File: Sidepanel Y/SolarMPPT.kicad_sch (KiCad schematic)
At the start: 38 parts, among them U11 INA180A4, U12 INA180A4

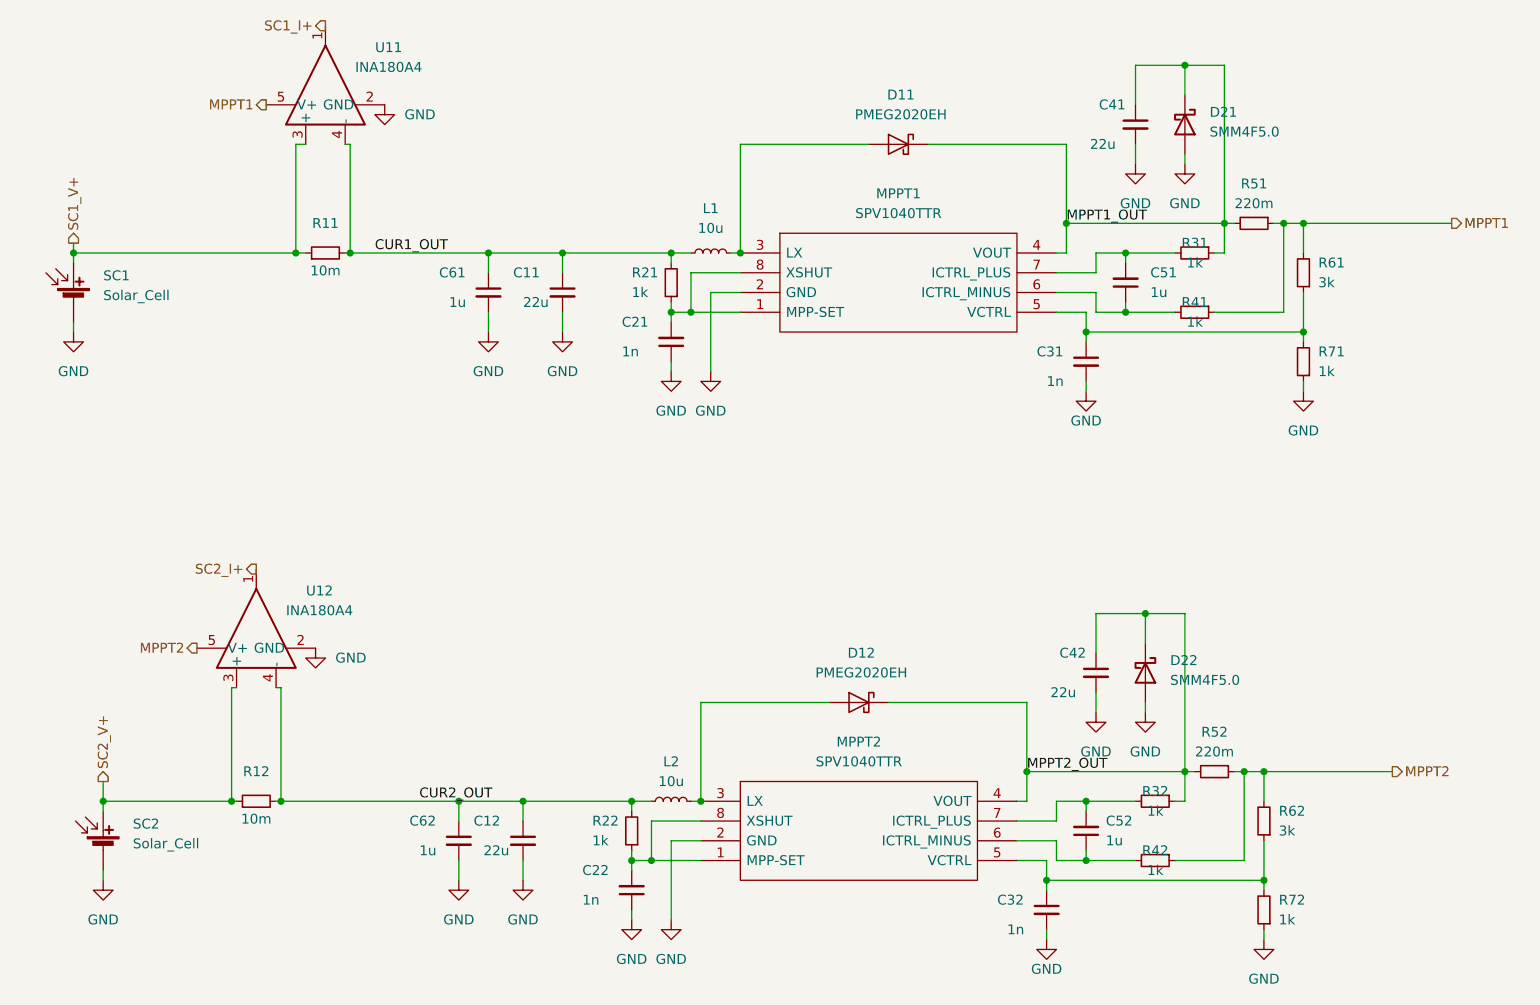
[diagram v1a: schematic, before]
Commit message: mirror the pinout of the connector on the Z- panel, split output capacitor in two capacitors
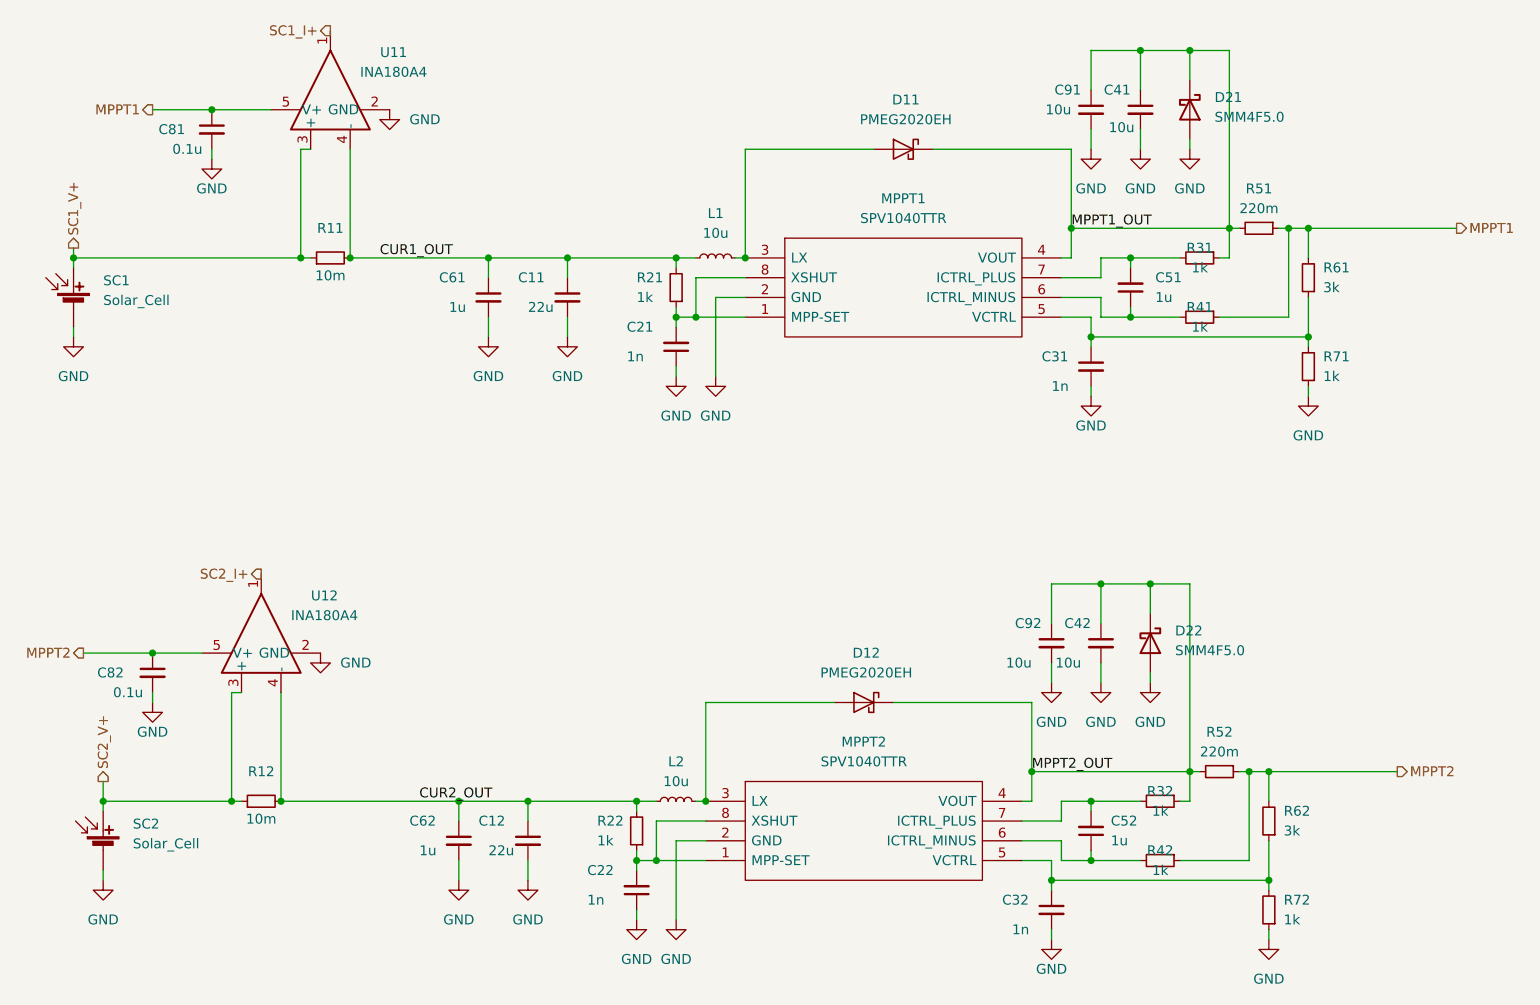
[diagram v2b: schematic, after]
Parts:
- added C81, C82: 0.1u, Capacitor_SMD:C_0603_1608Metric, symbol Device:C_Small
- added C91, C92: 10u, Capacitor_SMD:C_0805_2012Metric, symbol Device:C_Small
- C41, C42: value 22u -> 10u
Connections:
- net GND: now also C81.2, C82.2, C91.2, C92.2
- net MPPT1: now also C81.1
- net MPPT1_OUT: now also C91.1
- net MPPT2: now also C82.1
- net MPPT2_OUT: now also C92.1
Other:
- moved on the sheet: C11, C12, C21, C22, C31, C32, C41, C42, C51, C52, C61, D11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
